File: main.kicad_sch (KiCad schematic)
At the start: 0 parts

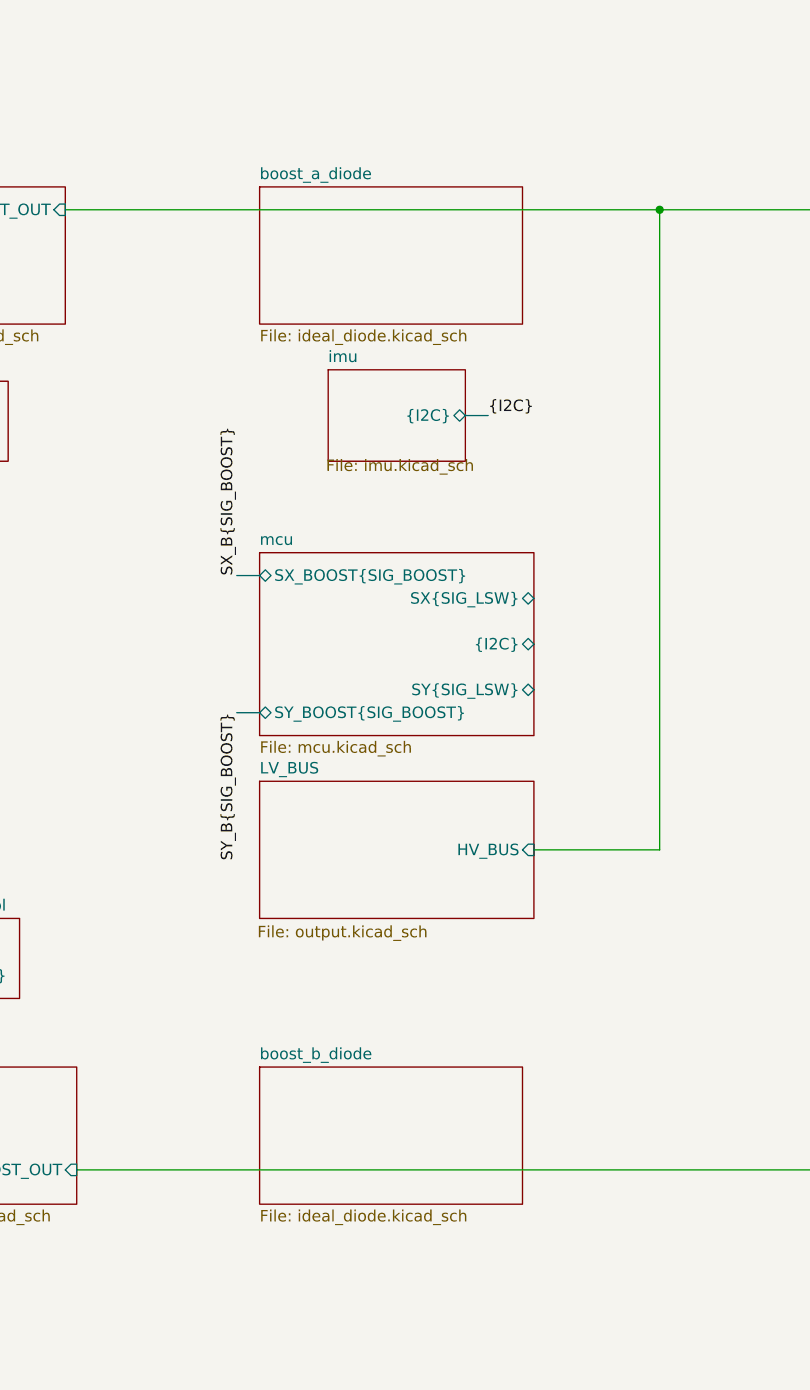
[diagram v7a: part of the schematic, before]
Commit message: Eiditng frontend
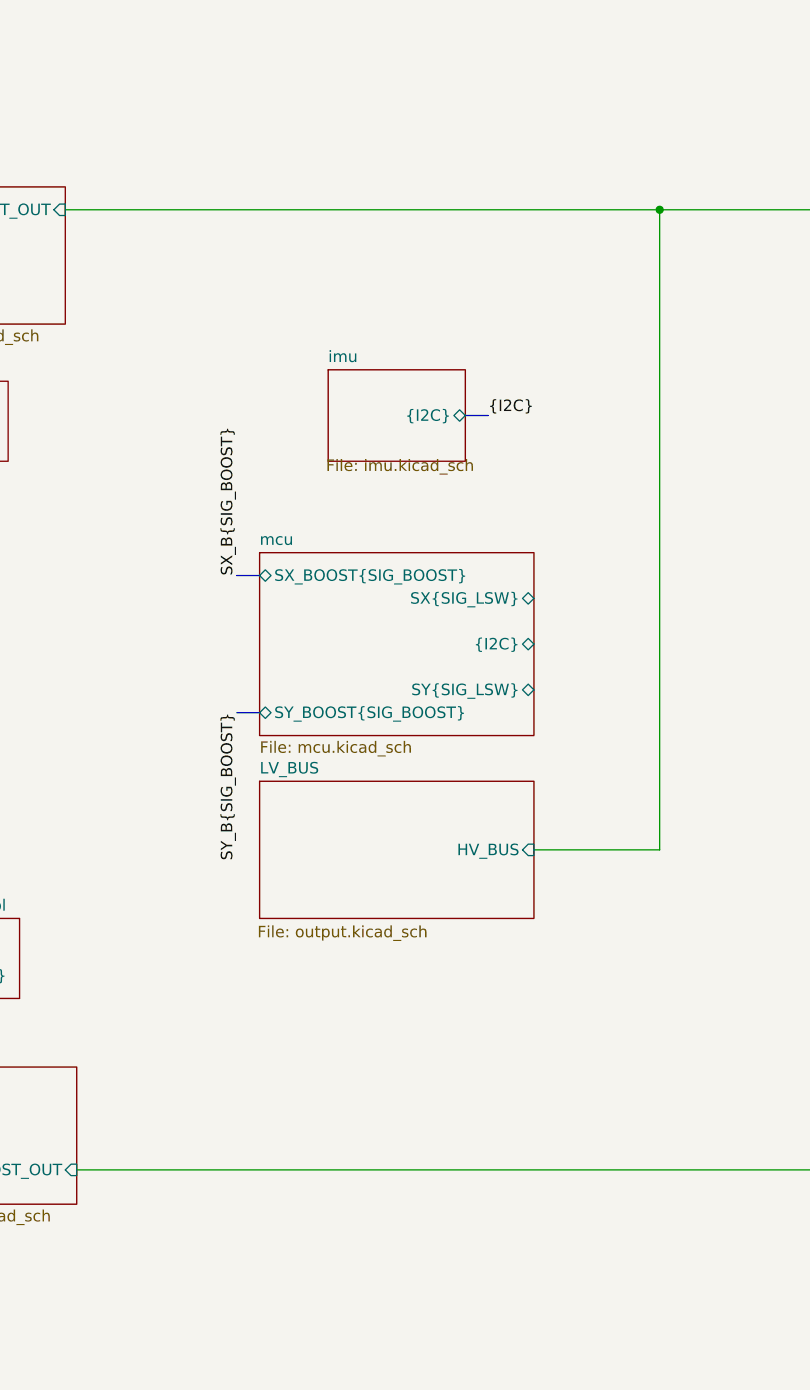
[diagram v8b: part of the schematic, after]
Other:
- removed sheet boost_a_diode
- removed sheet boost_b_diode
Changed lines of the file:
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@@
-	)
-	(sheet
-		(at 162.56 104.14)
-		(size 29.21 15.24)
-		(exclude_from_sim no)
-		(in_bom yes)
-		(on_board yes)
-		(dnp no)
-		(fields_autoplaced yes)
-		(stroke
-			(width 0.1524)
-			(type solid)
-		)
-		(fill
-			(color 0 0 0 0.0000)
-		)
-		(property "Sheetname" "boost_a_diode"
-			(at 162.56 103.4284 0)
-			(effects
-				(font
-					(size 1.27 1.27)
-				)
-				(justify left bottom)
-			)
-		)
-		(property "Sheetfile" "ideal_diode.kicad_sch"
-			(at 162.56 119.9646 0)
-			(effects
-				(font
-					(size 1.27 1.27)
-				)
-				(justify left top)
-			)
-		)
-		(instances
-			(project "PowerBoard"
-				(path "/99785679-20de-4827-b4cc-bc3c187068c9/9564929a-642e-4163-88c2-45054b63a5ed"
-					(page "19")
-				)
-			)
-		)
 	)
 	(sheet
@@
 				)
 			)
-		)
-	)
-	(sheet
-		(at 162.56 201.93)
-		(size 29.21 15.24)
-		(exclude_from_sim no)
-		(in_bom yes)
-		(on_board yes)
-		(dnp no)
-		(fields_autoplaced yes)
-		(stroke
-			(width 0.1524)
-			(type solid)
-		)
-		(fill
-			(color 0 0 0 0.0000)
-		)
-		(property "Sheetname" "boost_b_diode"
-			(at 162.56 201.2184 0)
-			(effects
-				(font
-					(size 1.27 1.27)
-				)
-				(justify left bottom)
-			)
-		)
-		(property "Sheetfile" "ideal_diode.kicad_sch"
-			(at 162.56 217.7546 0)
-			(effects
-				(font
-					(size 1.27 1.27)
-				)
-				(justify left top)
-			)
-		)
-		(instances
-			(project "PowerBoard"
-				(path "/99785679-20de-4827-b4cc-bc3c187068c9/9564929a-642e-4163-88c2-45054b63a5ed"
-					(page "7")
-				)
-			)
